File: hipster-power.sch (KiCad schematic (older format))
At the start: 22 parts, among them Q3 FDN340P, Q4 FDN340P, SW3 ON|OFF, U3 NCP5501, U4 CN3063, U5 MCP6002

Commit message: Now with less Hipster :(
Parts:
- removed C17: 10uF, Capacitors_SMD:C_0805_HandSoldering, symbol C
- removed C18: 0.1uF, Capacitors_SMD:C_0603_HandSoldering, symbol C
- removed Q3, Q4: FDN340P, TO_SOT_Packages_SMD:SOT-23_Handsoldering, symbol Q_PMOS_GSD
- removed R13: 3.6K (1%), Resistors_SMD:R_0603_HandSoldering, symbol R
- removed R14, R15: 100K, Resistors_SMD:R_0603_HandSoldering, symbol R
- removed TH1: 10K NTC, Capacitors_SMD:C_0603_HandSoldering, symbol THERMISTOR
- removed U4: CN3063, libs:CN3063_SOIC8_EP, symbol CN3063
- removed U5: MCP6002, libs:SO08_4mm, symbol MCP6002
- added U4: MCP73831, TO_SOT_Packages_SMD:SOT-23-5_HandSoldering, symbol MCP73831
- C13, C16: value 10uF -> 4u7
- R12: value 3.6K (1%) -> 2K
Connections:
- net labels added: UNREG_V
- net labels removed: 3.3V, GBAT
- wire segments 65 -> 33
- no-connect marks 1 -> 0
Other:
- moved on the sheet: C13, C14, C15, D2, D3, D4, R10, R11, R12, SW3, U3

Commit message: Added some digikey links.
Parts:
- C14: Digikey PN (none) -> 311-1088-1-ND; Link (none) -> http://www.digikey.com.au/product-detail/en/yageo/CC0603KRX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; Manufactur PN (none) -> CC0603KRX7R7BB104; Unit Cost (none) -> 0.10
- C15: Digikey PN (none) -> 490-7217-1-ND; Link (none) -> http://www.digikey.com.au/product-detail/en/murata-electron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; Manufacturer PN (none) -> GRM31CR60J107ME39K; Unit Cost (none) -> 0.60
- U3: Digikey PN (none) -> NCP5501DT33RKGOSCT-ND; Link (none) -> http://www.digikey.com.au/product-detail/en/on-semiconducto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; Manufacture PN (none) -> NCP5501DT33RKG; Unit Cost (none) -> 0.67
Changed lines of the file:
@@
 F 2 "libs:DPAK3.NCP5501" H 3900 4400 50  0001 C CNN
 F 3 "" H 3900 4400 50  0000 C CNN
+F 4 "NCP5501DT33RKGOSCT-ND" H 3900 4400 60  0001 C CNN "Digikey PN"
+F 5 "http://www.digikey.com.au/product-detail/en/on-semiconductor/NCP5501DT33RKG/NCP5501DT33RKGOSCT-ND/3462404" H 3900 4400 60  0001 C CNN "Link"
+F 6 "NCP5501DT33RKG" H 3900 4400 60  0001 C CNN "Manufacture PN"
+F 7 "0.67" H 3900 4400 60  0001 C CNN "Unit Cost"
 	1    3900 4400
 	1    0    0    -1
@@
 F 2 "Capacitors_SMD:C_0603_HandSoldering" H 4438 4450 50  0001 C CNN
 F 3 "" H 4400 4600 50  0000 C CNN
+F 4 "311-1088-1-ND" H 4400 4600 60  0001 C CNN "Digikey PN"
+F 5 "http://www.digikey.com.au/product-detail/en/yageo/CC0603KRX7R7BB104/311-1088-1-ND/302998" H 4400 4600 60  0001 C CNN "Link"
+F 6 "CC0603KRX7R7BB104" H 4400 4600 60  0001 C CNN "Manufactur PN"
+F 7 "0.10" H 4400 4600 60  0001 C CNN "Unit Cost"
 	1    4400 4600
 	1    0    0    -1
@@
 F 2 "Capacitors_SMD:C_1210_HandSoldering" H 4788 4450 50  0001 C CNN
 F 3 "" H 4750 4600 50  0000 C CNN
+F 4 "490-7217-1-ND" H 4750 4600 60  0001 C CNN "Digikey PN"
+F 5 "http://www.digikey.com.au/product-detail/en/murata-electronics-north-america/GRM31CR60J107ME39K/490-7217-1-ND/3991203" H 4750 4600 60  0001 C CNN "Link"
+F 6 "GRM31CR60J107ME39K" H 4750 4600 60  0001 C CNN "Manufacturer PN"
+F 7 "0.60" H 4750 4600 60  0001 C CNN "Unit Cost"
 	1    4750 4600
 	1    0    0    -1

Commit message: updated touch sensors
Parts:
- D4: footprint LEDs:LED_0603 -> (none)
- R11: footprint Resistors_SMD:R_0603_HandSoldering -> (none)
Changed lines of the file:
@@
 F 0 "D4" H 5200 4650 50  0000 C CNN
 F 1 "POWER" H 5200 4450 50  0000 C CNN
-F 2 "LEDs:LED_0603" H 5200 4550 50  0001 C CNN
+F 2 "" H 5200 4550 50  0001 C CNN
 F 3 "" H 5200 4550 50  0000 C CNN
 	1    5200 4550
@@
 F 0 "R11" V 5100 4100 50  0000 C CNN
 F 1 "470R" V 5300 4100 50  0000 C CNN
-F 2 "Resistors_SMD:R_0603_HandSoldering" V 5130 4100 50  0001 C CNN
+F 2 "" V 5130 4100 50  0001 C CNN
 F 3 "" H 5200 4100 50  0000 C CNN
 	1    5200 4100

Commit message: Added eInk decoupling caps.
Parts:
- added D?: SS14, Diodes_SMD:D_SMA, symbol D_Schottky
- added Q?: S8050, symbol Q_NPN_BEC
- added R?: 10K, symbol R
- D3, D4: symbol LED -> LED-RESCUE-minimum-viable-badge
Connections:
- net GND: now also R?.2
- net USB_PWR: now also D?.2 (A), Q?.1 (B), R?.1
- net VBAT: now also Q?.3 (C); no longer SW3.1
- new net UNREG_V: D?.1 (K), Q?.2 (E), SW3.1
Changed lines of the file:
@@
 EESchema Schematic File Version 2
+LIBS:minimum-viable-badge-rescue
 LIBS:power
 LIBS:device
@@
 $EndComp
 $Comp
-L LED D3
+L LED-RESCUE-minimum-viable-badge D3
 U 1 1 59282B08
 P 3400 2900
+AR Path="/59282B08" Ref="D3"  Part="1"
+AR Path="/592826E7/59282B08" Ref="D3"  Part="1"
 F 0 "D3" H 3400 3000 50  0000 C CNN
 F 1 "CHRG" H 3400 2800 50  0000 C CNN
@@
 Text Label 2300 2550 0    60   ~ 0
 VIN
-Text HLabel 5500 2550 1    60   Input ~ 0
-VBAT
-Text Label 6050 2550 2    60   ~ 0
+Text Label 3500 1100 2    60   ~ 0
 UNREG_V
 $Comp
@@
 	1    0    0    -1
 $EndComp
-Text Label 2100 4350 0    60   ~ 0
+Text Label 1950 4350 0    60   ~ 0
 UNREG_V
 Wire Wire Line
-	2100 4350 2350 4350
+	1950 4350 2350 4350
 $Comp
 L NCP5501 U3
@@
 $EndComp
 $Comp
-L LED D4
+L LED-RESCUE-minimum-viable-badge D4
 U 1 1 59287320
 P 5200 4550
+AR Path="/59287320" Ref="D4"  Part="1"
+AR Path="/592826E7/59287320" Ref="D4"  Part="1"
 F 0 "D4" H 5200 4650 50  0000 C CNN
 F 1 "POWER" H 5200 4450 50  0000 C CNN
@@
 	5200 4350 5200 4250
 Wire Wire Line
-	4300 4350 4950 4350
+	4300 4350 4400 4350
+Wire Wire Line
+	4400 4350 4750 4350
+Wire Wire Line
+	4750 4350 4950 4350
 Wire Wire Line
 	4950 4350 4950 3900
 Wire Wire Line
-	4950 3900 5450 3900
+	4950 3900 5200 3900
+Wire Wire Line
+	5200 3900 5450 3900
 Wire Wire Line
 	5200 3900 5200 3950
@@
 Connection ~ 4400 4350
 Wire Wire Line
-	3900 4650 3900 4900
-Wire Wire Line
-	3900 4850 5200 4850
+	3900 4650 3900 4850
+Wire Wire Line
+	3900 4850 3900 4900
+Wire Wire Line
+	3900 4850 4400 4850
+Wire Wire Line
+	4400 4850 4750 4850
+Wire Wire Line
+	4750 4850 5200 4850
 Wire Wire Line
 	4400 4850 4400 4750
@@
 $EndComp
 Wire Wire Line
-	2850 2550 3950 2550
+	2850 2550 2950 2550
+Wire Wire Line
+	2950 2550 3400 2550
+Wire Wire Line
+	3400 2550 3950 2550
 Wire Wire Line
 	3400 2700 3400 2550
@@
 	4750 2750 4800 2750
 Wire Wire Line
-	4800 2750 4800 3100
+	4800 2750 4800 3050
+Wire Wire Line
+	4800 3050 4800 3100
 Wire Wire Line
 	4800 3050 5000 3050
@@
 	5300 3100 5300 3000
 Wire Wire Line
-	4750 2550 6050 2550
+	4750 2550 5300 2550
+Wire Wire Line
+	5300 2550 5550 2550
 Wire Wire Line
 	5300 2550 5300 2700
 Connection ~ 5300 2550
+$Comp
+L Q_NPN_BEC Q?
+U 1 1 59A0FD5C
+P 2650 1200
+F 0 "Q?" H 2550 1350 50  0000 R CNN
+F 1 "S8050" V 2850 1300 50  0000 R CNN
+F 2 "" H 2850 1300 50  0000 C CNN
+F 3 "" H 2650 1200 50  0000 C CNN
+	1    2650 1200
+	0    -1   -1   0
+$EndComp
+Text HLabel 2250 1100 0    60   Input ~ 0
+VBAT
+Text Label 3500 1450 2    60   ~ 0
+VIN
+$Comp
+L D_Schottky D?
+U 1 1 59A10ECB
+P 3000 1250
+F 0 "D?" H 3000 1350 50  0000 C CNN
+F 1 "SS14" H 3000 1150 50  0000 C CNN
+F 2 "Diodes_SMD:D_SMA" H 3000 1250 50  0001 C CNN
+F 3 "" H 3000 1250 50  0000 C CNN
+	1    3000 1250
+	0    1    1    0
+$EndComp
+$Comp
+L GND #PWR?
+U 1 1 59A1135B
+P 2650 1900
+F 0 "#PWR?" H 2650 1650 50  0001 C CNN
+F 1 "GND" H 2650 1750 50  0000 C CNN
+F 2 "" H 2650 1900 50  0000 C CNN
+F 3 "" H 2650 1900 50  0000 C CNN
+	1    2650 1900
+	1    0    0    -1
+$EndComp
+$Comp
+L R R?
+U 1 1 59A11654
+P 2650 1650
+F 0 "R?" V 2550 1650 50  0000 C CNN
+F 1 "10K" V 2750 1650 50  0000 C CNN
+F 2 "" V 2580 1650 50  0001 C CNN
+F 3 "" H 2650 1650 50  0000 C CNN
+	1    2650 1650
+	1    0    0    -1
+$EndComp
+Wire Wire Line
+	2250 1100 2450 1100
+Wire Wire Line
+	2850 1100 3000 1100
+Wire Wire Line
+	3000 1100 3500 1100
+Connection ~ 3000 1100
+Wire Wire Line
+	2650 1400 2650 1450
+Wire Wire Line
+	2650 1450 2650 1500
+Wire Wire Line
+	2650 1450 3000 1450
+Wire Wire Line
+	3000 1450 3500 1450
+Wire Wire Line
+	3000 1400 3000 1450
+Connection ~ 3000 1450
+Connection ~ 2650 1450
+Wire Wire Line
+	2650 1800 2650 1900
+Text Label 2250 1100 0    60   ~ 0
+VBAT
+Text Label 5550 2550 2    60   ~ 0
+VBAT
 $EndSCHEMATC

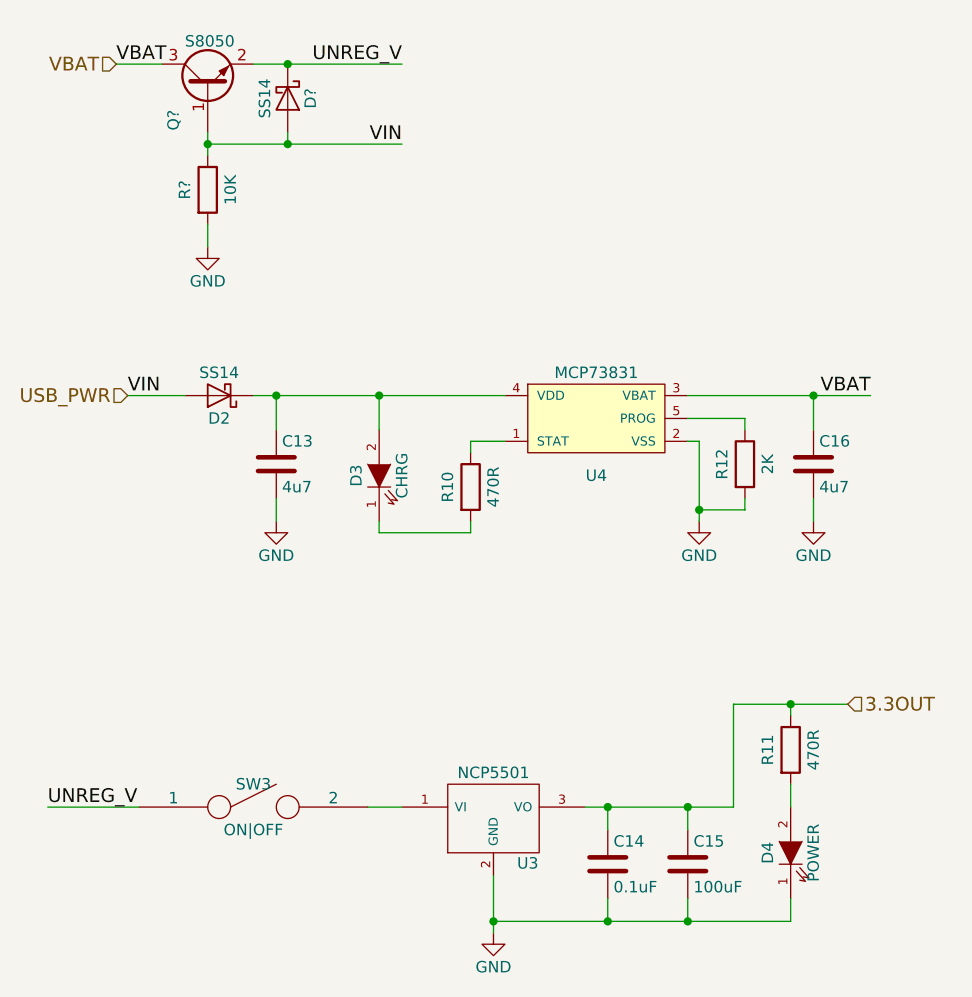
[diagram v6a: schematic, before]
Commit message: Extra touch buttons
and edge connector!
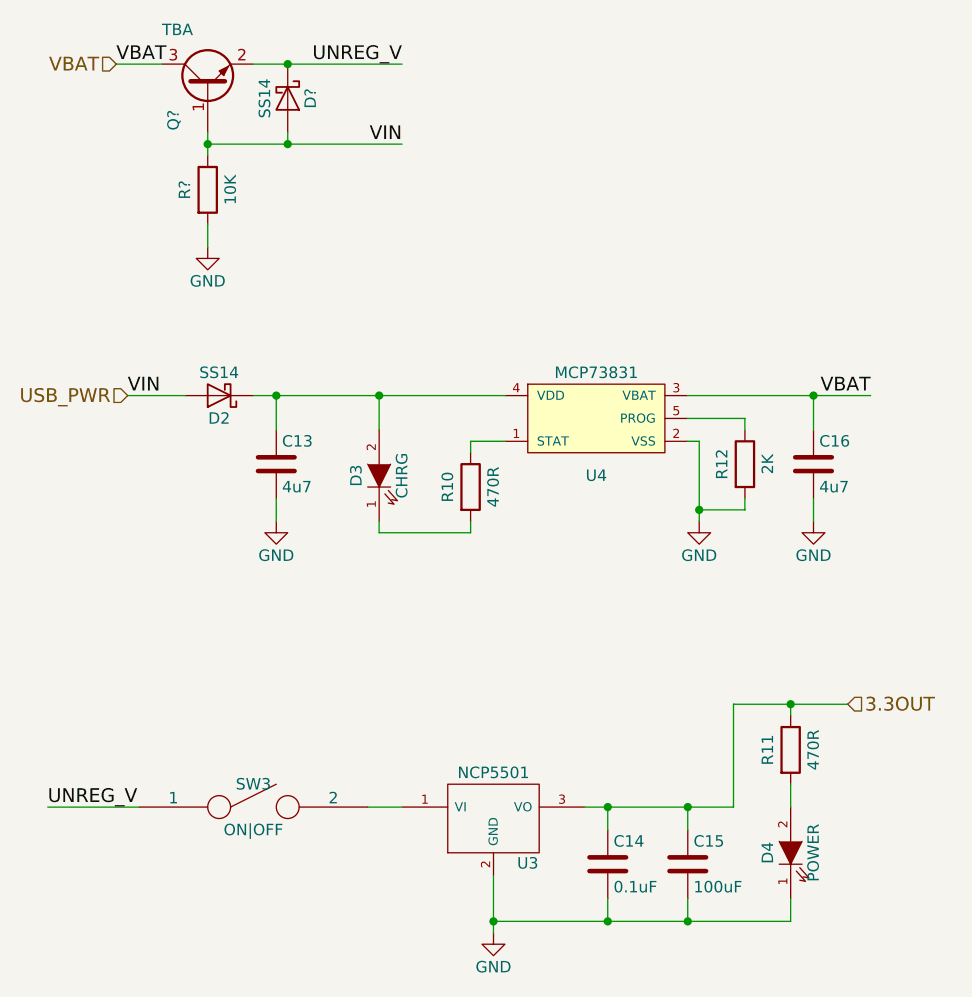
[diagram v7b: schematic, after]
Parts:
- Q?: value S8050 -> TBA
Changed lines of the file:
@@
 	5200 4350 5200 4250
 Wire Wire Line
-	4300 4350 4400 4350
-Wire Wire Line
-	4400 4350 4750 4350
-Wire Wire Line
-	4750 4350 4950 4350
+	4300 4350 4950 4350
 Wire Wire Line
 	4950 4350 4950 3900
 Wire Wire Line
-	4950 3900 5200 3900
-Wire Wire Line
-	5200 3900 5450 3900
+	4950 3900 5450 3900
 Wire Wire Line
 	5200 3900 5200 3950
@@
 Connection ~ 4400 4350
 Wire Wire Line
-	3900 4650 3900 4850
+	3900 4650 3900 4900
 Wire Wire Line
-	3900 4850 3900 4900
-Wire Wire Line
-	3900 4850 4400 4850
-Wire Wire Line
-	4400 4850 4750 4850
-Wire Wire Line
-	4750 4850 5200 4850
+	3900 4850 5200 4850
 Wire Wire Line
 	4400 4850 4400 4750
@@
 $EndComp
 Wire Wire Line
-	2850 2550 2950 2550
-Wire Wire Line
-	2950 2550 3400 2550
-Wire Wire Line
-	3400 2550 3950 2550
+	2850 2550 3950 2550
 Wire Wire Line
 	3400 2700 3400 2550
@@
 	4750 2750 4800 2750
 Wire Wire Line
-	4800 2750 4800 3050
-Wire Wire Line
-	4800 3050 4800 3100
+	4800 2750 4800 3100
 Wire Wire Line
 	4800 3050 5000 3050
@@
 	5300 3100 5300 3000
 Wire Wire Line
-	4750 2550 5300 2550
-Wire Wire Line
-	5300 2550 5550 2550
+	4750 2550 5550 2550
 Wire Wire Line
 	5300 2550 5300 2700
@@
 P 2650 1200
 F 0 "Q?" H 2550 1350 50  0000 R CNN
-F 1 "S8050" V 2850 1300 50  0000 R CNN
+F 1 "TBA" V 2900 1400 50  0000 R CNN
 F 2 "" H 2850 1300 50  0000 C CNN
 F 3 "" H 2650 1200 50  0000 C CNN
@@
 	2250 1100 2450 1100
 Wire Wire Line
-	2850 1100 3000 1100
-Wire Wire Line
-	3000 1100 3500 1100
+	2850 1100 3500 1100
 Connection ~ 3000 1100
 Wire Wire Line
-	2650 1400 2650 1450
+	2650 1400 2650 1500
 Wire Wire Line
-	2650 1450 2650 1500
-Wire Wire Line
-	2650 1450 3000 1450
-Wire Wire Line
-	3000 1450 3500 1450
+	2650 1450 3500 1450
 Wire Wire Line
 	3000 1400 3000 1450

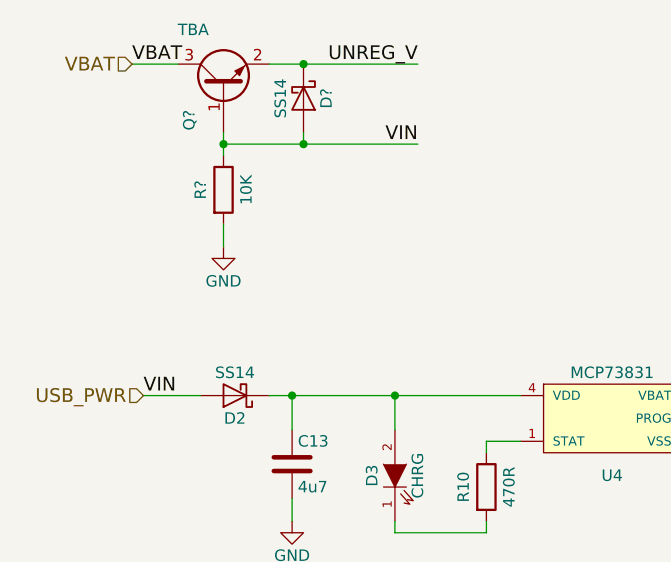
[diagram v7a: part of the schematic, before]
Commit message: power: Swap BJT for FET in power selection circuit
Went with FDN340P as used on ESPlant, but any appropriately rated FET will do.

Closes #12
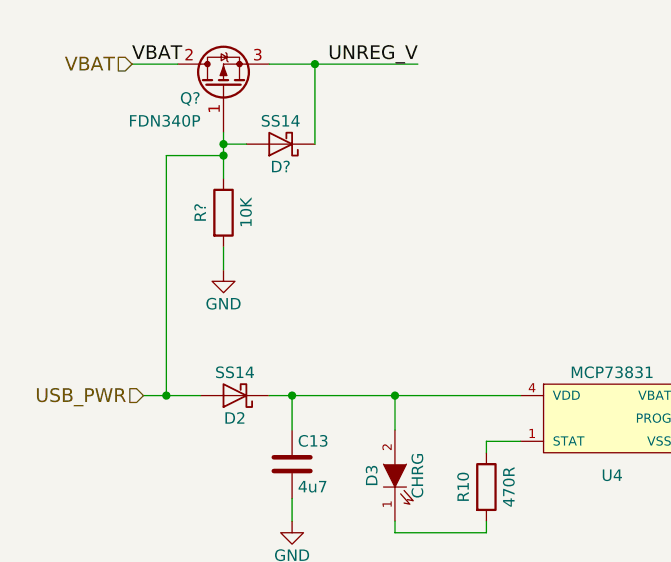
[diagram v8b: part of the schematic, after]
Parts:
- removed Q?: TBA, symbol Q_NPN_BEC
- added Q?: FDN340P, symbol Q_PMOS_GDS
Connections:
- net UNREG_V: now also Q?.3 (S)
- net USB_PWR: now also Q?.1 (G)
- net VBAT: now also Q?.2 (D)
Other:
- moved on the sheet: D?, R?
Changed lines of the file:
@@
 USB_PWR
-$Comp
-L D_Schottky D2
-U 1 1 592829A1
-P 2700 2550
-F 0 "D2" H 2700 2650 50  0000 C CNN
-F 1 "SS14" H 2700 2450 50  0000 C CNN
-F 2 "Diodes_SMD:D_SMA" H 2700 2550 50  0001 C CNN
-F 3 "" H 2700 2550 50  0000 C CNN
-	1    2700 2550
-	-1   0    0    1
-$EndComp
-Wire Wire Line
-	2300 2550 2550 2550
 $Comp
 L R R10
@@
 	1    0    0    -1
 $EndComp
-Wire Wire Line
-	2950 3100 2950 3000
-Wire Wire Line
-	2950 2550 2950 2700
-Connection ~ 2950 2550
 $Comp
 L R R12
@@
 	1    0    0    -1
 $EndComp
-Text Label 2300 2550 0    60   ~ 0
-VIN
 Text Label 3500 1100 2    60   ~ 0
 UNREG_V
@@
 Text Label 1950 4350 0    60   ~ 0
 UNREG_V
-Wire Wire Line
-	1950 4350 2350 4350
 $Comp
 L NCP5501 U3
@@
 	1    0    0    -1
 $EndComp
-Wire Wire Line
-	3350 4350 3500 4350
 $Comp
 L C C14
@@
 	1    0    0    -1
 $EndComp
-Wire Wire Line
-	5200 4350 5200 4250
-Wire Wire Line
-	4300 4350 4950 4350
-Wire Wire Line
-	4950 4350 4950 3900
-Wire Wire Line
-	4950 3900 5450 3900
-Wire Wire Line
-	5200 3900 5200 3950
-Wire Wire Line
-	4750 4450 4750 4350
-Connection ~ 4750 4350
-Wire Wire Line
-	4400 4450 4400 4350
-Connection ~ 4400 4350
-Wire Wire Line
-	3900 4650 3900 4900
-Wire Wire Line
-	3900 4850 5200 4850
-Wire Wire Line
-	4400 4850 4400 4750
-Wire Wire Line
-	4750 4850 4750 4750
-Connection ~ 4400 4850
-Wire Wire Line
-	5200 4850 5200 4750
-Connection ~ 4750 4850
-Connection ~ 3900 4850
 $Comp
 L GND #PWR22
@@
 Text HLabel 5450 3900 2    60   Input ~ 0
 3.3OUT
-Connection ~ 5200 3900
 $Comp
 L MCP73831 U4
@@
 	1    0    0    -1
 $EndComp
-Wire Wire Line
-	2850 2550 3950 2550
-Wire Wire Line
-	3400 2700 3400 2550
-Connection ~ 3400 2550
-Wire Wire Line
-	3950 2750 3800 2750
-Wire Wire Line
-	3800 2750 3800 2800
-Wire Wire Line
-	3800 3100 3800 3150
-Wire Wire Line
-	3800 3150 3400 3150
-Wire Wire Line
-	3400 3150 3400 3100
-Wire Wire Line
-	4750 2650 5000 2650
-Wire Wire Line
-	5000 2650 5000 2700
-Wire Wire Line
-	4750 2750 4800 2750
-Wire Wire Line
-	4800 2750 4800 3100
-Wire Wire Line
-	4800 3050 5000 3050
-Wire Wire Line
-	5000 3050 5000 3000
 $Comp
 L GND #PWR23
@@
 	1    0    0    -1
 $EndComp
-Connection ~ 4800 3050
 $Comp
 L C C16
@@
 	1    0    0    -1
 $EndComp
-Wire Wire Line
-	5300 3100 5300 3000
-Wire Wire Line
-	4750 2550 5550 2550
-Wire Wire Line
-	5300 2550 5300 2700
-Connection ~ 5300 2550
-$Comp
-L Q_NPN_BEC Q?
-U 1 1 59A0FD5C
-P 2650 1200
-F 0 "Q?" H 2550 1350 50  0000 R CNN
-F 1 "TBA" V 2900 1400 50  0000 R CNN
-F 2 "" H 2850 1300 50  0000 C CNN
-F 3 "" H 2650 1200 50  0000 C CNN
-	1    2650 1200
-	0    -1   -1   0
-$EndComp
 Text HLabel 2250 1100 0    60   Input ~ 0
 VBAT
-Text Label 3500 1450 2    60   ~ 0
-VIN
 $Comp
 L D_Schottky D?
 U 1 1 59A10ECB
-P 3000 1250
-F 0 "D?" H 3000 1350 50  0000 C CNN
-F 1 "SS14" H 3000 1150 50  0000 C CNN
-F 2 "Diodes_SMD:D_SMA" H 3000 1250 50  0001 C CNN
-F 3 "" H 3000 1250 50  0000 C CNN
-	1    3000 1250
-	0    1    1    0
+P 2900 1450
+F 0 "D?" H 2900 1550 50  0000 C CNN
+F 1 "SS14" H 2900 1350 50  0000 C CNN
+F 2 "Diodes_SMD:D_SMA" H 2900 1450 50  0001 C CNN
+F 3 "" H 2900 1450 50  0000 C CNN
+	1    2900 1450
+	-1   0    0    1
 $EndComp
 $Comp
 L GND #PWR?
 U 1 1 59A1135B
-P 2650 1900
-F 0 "#PWR?" H 2650 1650 50  0001 C CNN
-F 1 "GND" H 2650 1750 50  0000 C CNN
-F 2 "" H 2650 1900 50  0000 C CNN
-F 3 "" H 2650 1900 50  0000 C CNN
-	1    2650 1900
+P 2650 2000
+F 0 "#PWR?" H 2650 1750 50  0001 C CNN
+F 1 "GND" H 2650 1850 50  0000 C CNN
+F 2 "" H 2650 2000 50  0000 C CNN
+F 3 "" H 2650 2000 50  0000 C CNN
+	1    2650 2000
 	1    0    0    -1
 $EndComp
@@
 L R R?
 U 1 1 59A11654
-P 2650 1650
-F 0 "R?" V 2550 1650 50  0000 C CNN
-F 1 "10K" V 2750 1650 50  0000 C CNN
-F 2 "" V 2580 1650 50  0001 C CNN
-F 3 "" H 2650 1650 50  0000 C CNN
-	1    2650 1650
-	1    0    0    -1
-$EndComp
-Wire Wire Line
-	2250 1100 2450 1100
-Wire Wire Line
-	2850 1100 3500 1100
-Connection ~ 3000 1100
-Wire Wire Line
-	2650 1400 2650 1500
-Wire Wire Line
-	2650 1450 3500 1450
-Wire Wire Line
-	3000 1400 3000 1450
-Connection ~ 3000 1450
-Connection ~ 2650 1450
-Wire Wire Line
-	2650 1800 2650 1900
+P 2650 1750
+F 0 "R?" V 2550 1750 50  0000 C CNN
+F 1 "10K" V 2750 1750 50  0000 C CNN
+F 2 "" V 2580 1750 50  0001 C CNN
+F 3 "" H 2650 1750 50  0000 C CNN
+	1    2650 1750
+	1    0    0    -1
+$EndComp
 Text Label 2250 1100 0    60   ~ 0
 VBAT
 Text Label 5550 2550 2    60   ~ 0
 VBAT
+$Comp
+L Q_PMOS_GDS Q?
+U 1 1 59A3FE7A
+P 2650 1200
+F 0 "Q?" V 2600 1300 50  0000 L CNN
+F 1 "FDN340P" V 2500 1300 50  0000 L CNN
+F 2 "" H 2850 1300 50  0001 C CNN
+F 3 "" H 2650 1200 50  0001 C CNN
+	1    2650 1200
+	0    -1   -1   0
+$EndComp
+Wire Wire Line
+	2300 2550 2550 2550
+Wire Wire Line
+	2950 3100 2950 3000
+Wire Wire Line
+	2950 2550 2950 2700
+Connection ~ 2950 2550
+Wire Wire Line
+	1950 4350 2350 4350
+Wire Wire Line
+	3350 4350 3500 4350
+Wire Wire Line
+	5200 4350 5200 4250
+Wire Wire Line
+	4300 4350 4950 4350
+Wire Wire Line
+	4950 4350 4950 3900
+Wire Wire Line
+	4950 3900 5450 3900
+Wire Wire Line
+	5200 3900 5200 3950
+Wire Wire Line
+	4750 4450 4750 4350
+Connection ~ 4750 4350
+Wire Wire Line
+	4400 4450 4400 4350
+Connection ~ 4400 4350
+Wire Wire Line
+	3900 4650 3900 4900
+Wire Wire Line
+	3900 4850 5200 4850
+Wire Wire Line
+	4400 4850 4400 4750
+Wire Wire Line
+	4750 4850 4750 4750
+Connection ~ 4400 4850
+Wire Wire Line
+	5200 4850 5200 4750
+Connection ~ 4750 4850
+Connection ~ 3900 4850
+Connection ~ 5200 3900
+Wire Wire Line
+	2850 2550 3950 2550
+Wire Wire Line
+	3400 2700 3400 2550
+Connection ~ 3400 2550
+Wire Wire Line
+	3950 2750 3800 2750
+Wire Wire Line
+	3800 2750 3800 2800
+Wire Wire Line
+	3800 3100 3800 3150
+Wire Wire Line
+	3800 3150 3400 3150
+Wire Wire Line
+	3400 3150 3400 3100
+Wire Wire Line
+	4750 2650 5000 2650
+Wire Wire Line
+	5000 2650 5000 2700
+Wire Wire Line
+	4750 2750 4800 2750
+Wire Wire Line
+	4800 2750 4800 3100
+Wire Wire Line
+	4800 3050 5000 3050
+Wire Wire Line
+	5000 3050 5000 3000
+Connection ~ 4800 3050
+Wire Wire Line
+	5300 3100 5300 3000
+Wire Wire Line
+	4750 2550 5550 2550
+Wire Wire Line
+	5300 2550 5300 2700
+Connection ~ 5300 2550
+Wire Wire Line
+	2250 1100 2450 1100
+Wire Wire Line
+	2850 1100 3500 1100
+Wire Wire Line
+	2650 1400 2650 1600
+Wire Wire Line
+	3050 1450 3050 1100
+Connection ~ 3050 1100
+Connection ~ 2650 1500
+Wire Wire Line
+	2650 2000 2650 1900
+Wire Wire Line
+	2750 1450 2650 1450
+Connection ~ 2650 1450
+$Comp
+L D_Schottky D2
+U 1 1 592829A1
+P 2700 2550
+F 0 "D2" H 2700 2650 50  0000 C CNN
+F 1 "SS14" H 2700 2450 50  0000 C CNN
+F 2 "Diodes_SMD:D_SMA" H 2700 2550 50  0001 C CNN
+F 3 "" H 2700 2550 50  0000 C CNN
+	1    2700 2550
+	-1   0    0    1
+$EndComp
+Connection ~ 2400 2550
+Wire Wire Line
+	2650 1500 2400 1500
+Wire Wire Line
+	2400 1500 2400 2550
 $EndSCHEMATC
